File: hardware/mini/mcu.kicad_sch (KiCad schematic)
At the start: 36 parts, among them U5 RP2040, U6 W25Q128JVP, Y1 12 MHz ABM8-272-T3

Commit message: route power stage
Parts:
- removed TP4: P16, TestPoint:TestPoint_Pad_D1.0mm, symbol Connector:TestPoint
- added R52, R53: 100k, Resistor_SMD:R_0402_1005Metric, symbol Device:R
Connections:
- net P16 is gone; now on net DISP_BACKLIGHT: U5.27 (GPIO16)
- net ROW_3 is gone; now on net ROW_2: U5.13 (GPIO10)
- net ROW_4 is gone; now on net LED_DATA: U5.14 (GPIO11)
- net +3V3: now also R52.2, R53.2
- net DISP_BACKLIGHT: no longer U5.18 (GPIO15)
- net LED_DATA: no longer U5.17 (GPIO14)
- net ROW_0: now also U5.11 (GPIO8); no longer U5.9 (GPIO7)
- net ROW_1: now also U5.12 (GPIO9); no longer U5.11 (GPIO8)
- net ROW_2: no longer U5.12 (GPIO9)
- new net COL_2: U5.9 (GPIO7)
- new net CONVERTER_INT_A: R52.1, U5.17 (GPIO14)
- new net CONVERTER_INT_B: R53.1, U5.18 (GPIO15)
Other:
- note removed: "BUTTON MATRIX"
- moved on the sheet: R20, R23

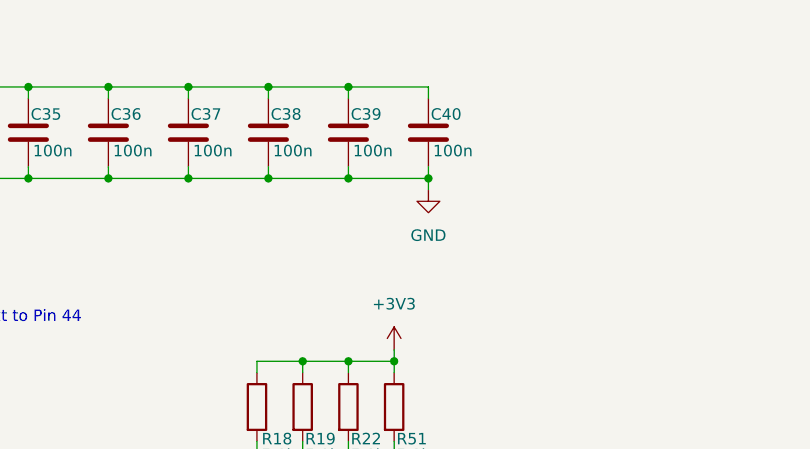
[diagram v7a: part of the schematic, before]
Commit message: route digitals
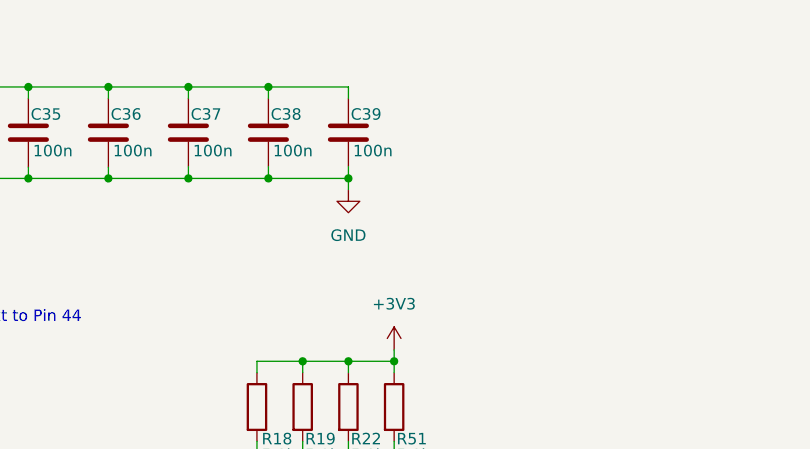
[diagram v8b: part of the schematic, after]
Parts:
- removed C40: 100n, Capacitor_SMD:C_0402_1005Metric, symbol Device:C
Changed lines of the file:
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@@
 	)
 	(junction
-		(at 157.48 43.18)
-		(diameter 0)
-		(color 0 0 0 0)
-	)
-	(junction
 		(at 157.48 120.65)
 		(diameter 0)
@@
 	)
 	(junction
-		(at 166.37 53.34)
-		(diameter 0)
-		(color 0 0 0 0)
-	)
-	(junction
 		(at 261.62 123.19)
 		(diameter 0)
@@
 	(wire
 		(pts
-			(xy 157.48 53.34) (xy 166.37 53.34)
-		)
-		(stroke
-			(width 0)
-			(type default)
-		)
-	)
-	(wire
-		(pts
 			(xy 55.88 118.11) (xy 67.31 118.11)
 		)
@@
 	(wire
 		(pts
-			(xy 166.37 44.45) (xy 166.37 43.18)
-		)
-		(stroke
-			(width 0)
-			(type default)
-		)
-	)
-	(wire
-		(pts
 			(xy 118.11 95.25) (xy 172.72 95.25)
 		)
@@
 	(wire
 		(pts
-			(xy 166.37 53.34) (xy 166.37 54.61)
+			(xy 157.48 53.34) (xy 157.48 54.61)
 		)
 		(stroke
@@
 	(wire
 		(pts
-			(xy 166.37 52.07) (xy 166.37 53.34)
-		)
-		(stroke
-			(width 0)
-			(type default)
-		)
-	)
-	(wire
-		(pts
 			(xy 118.11 143.51) (xy 162.56 143.51)
 		)
@@
 	(wire
 		(pts
-			(xy 157.48 43.18) (xy 166.37 43.18)
-		)
-		(stroke
-			(width 0)
-			(type default)
-		)
-	)
-	(wire
-		(pts
 			(xy 152.4 104.14) (xy 147.32 104.14)
 		)
@@
 	(symbol
 		(lib_id "power:GND")
-		(at 166.37 54.61 0)
+		(at 157.48 54.61 0)
 		(unit 1)
 		(exclude_from_sim no)
@@
 		(fields_autoplaced yes)
 		(property "Reference" "#PWR039"
-			(at 166.37 60.96 0)
+			(at 157.48 60.96 0)
 			(effects
 				(font
@@
 		)
 		(property "Value" "GND"
-			(at 166.37 59.69 0)
+			(at 157.48 59.69 0)
 			(effects
 				(font
@@
 		)
 		(property "Footprint" ""
-			(at 166.37 54.61 0)
+			(at 157.48 54.61 0)
 			(effects
 				(font
@@
 		)
 		(property "Datasheet" ""
-			(at 166.37 54.61 0)
+			(at 157.48 54.61 0)
 			(effects
 				(font
@@
 		)
 		(property "Description" "Power symbol creates a global label with name \"GND\" , ground"
-			(at 166.37 54.61 0)
+			(at 157.48 54.61 0)
 			(effects
 				(font
@@
 					(unit 1)
 				)
-			)
-		)
-	)
-	(symbol
-		(lib_id "Device:C")
-		(at 166.37 48.26 0)
-		(unit 1)
-		(exclude_from_sim no)
-		(in_bom yes)
-		(on_board yes)
-		(dnp no)
-		(property "Reference" "C40"
-			(at 166.624 46.228 0)
-			(effects
-				(font
-					(size 1.27 1.27)
-				)
-				(justify left)
-			)
-		)
-		(property "Value" "100n"
-			(at 166.878 50.292 0)
-			(effects
-				(font
-					(size 1.27 1.27)
-				)
-				(justify left)
-			)
-		)
-		(property "Footprint" "Capacitor_SMD:C_0402_1005Metric"
-			(at 167.3352 52.07 0)
-			(effects
-				(font
-					(size 1.27 1.27)
-				)
-				(hide yes)
-			)
-		)
-		(property "Datasheet" "~"
-			(at 166.37 48.26 0)
-			(effects
-				(font
-					(size 1.27 1.27)
-				)
-				(hide yes)
-			)
-		)
-		(property "Description" "Unpolarized capacitor"
-			(at 166.37 48.26 0)
-			(effects
-				(font
-					(size 1.27 1.27)
-				)
-				(hide yes)
-			)
-		)
-		(property "LCSC" "C307331"
-			(at 166.37 48.26 0)
-			(effects
-				(font
-					(size 1.27 1.27)
-				)
-				(hide yes)
-			)
-		)
-		(pin "2"
-		)
-		(pin "1"
-		)
-		(instances
-			(project "mini"
-				(path "/5aaaac9a-5acd-4aef-ad51-a6d04aa88705/8fbd1251-7beb-4aac-9406-53fe608f326c"
-					(reference "C40")
-					(unit 1)
-				)
